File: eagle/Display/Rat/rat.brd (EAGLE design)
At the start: 99.2 x 116.2 mm, 72 parts, among them IC1 4511D, IC2 MEGA128-A, IC3 PCA82C250T, IC4 74LS138D, IC5 74LS138D, IC6 LM3914V, IC7 LM3914V, Q1 18.4320 MHz

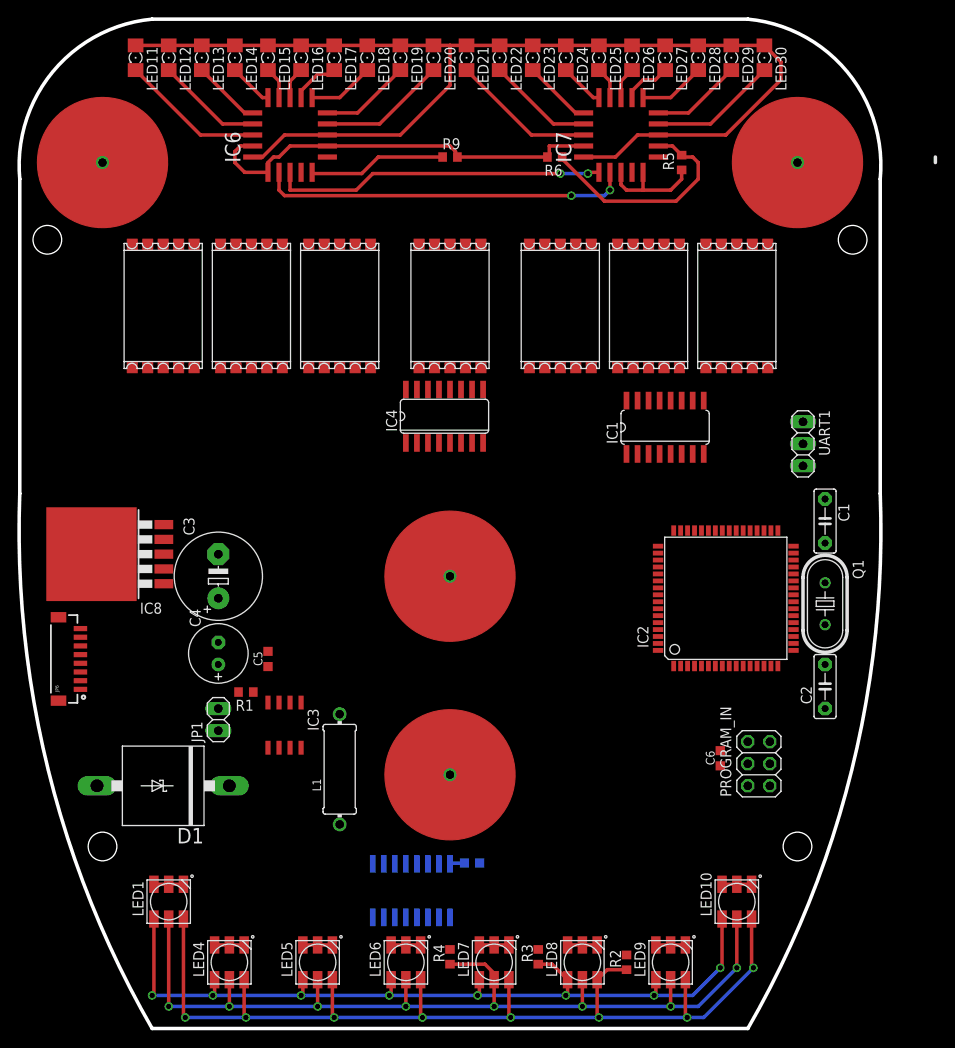
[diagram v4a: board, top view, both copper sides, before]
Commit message: changes to display layout
- Added shift light
- adjusted position of drillholes to take into account the size of the
buttons and the fotary switch
- added the connectors for the buttons (might have to be redonee)
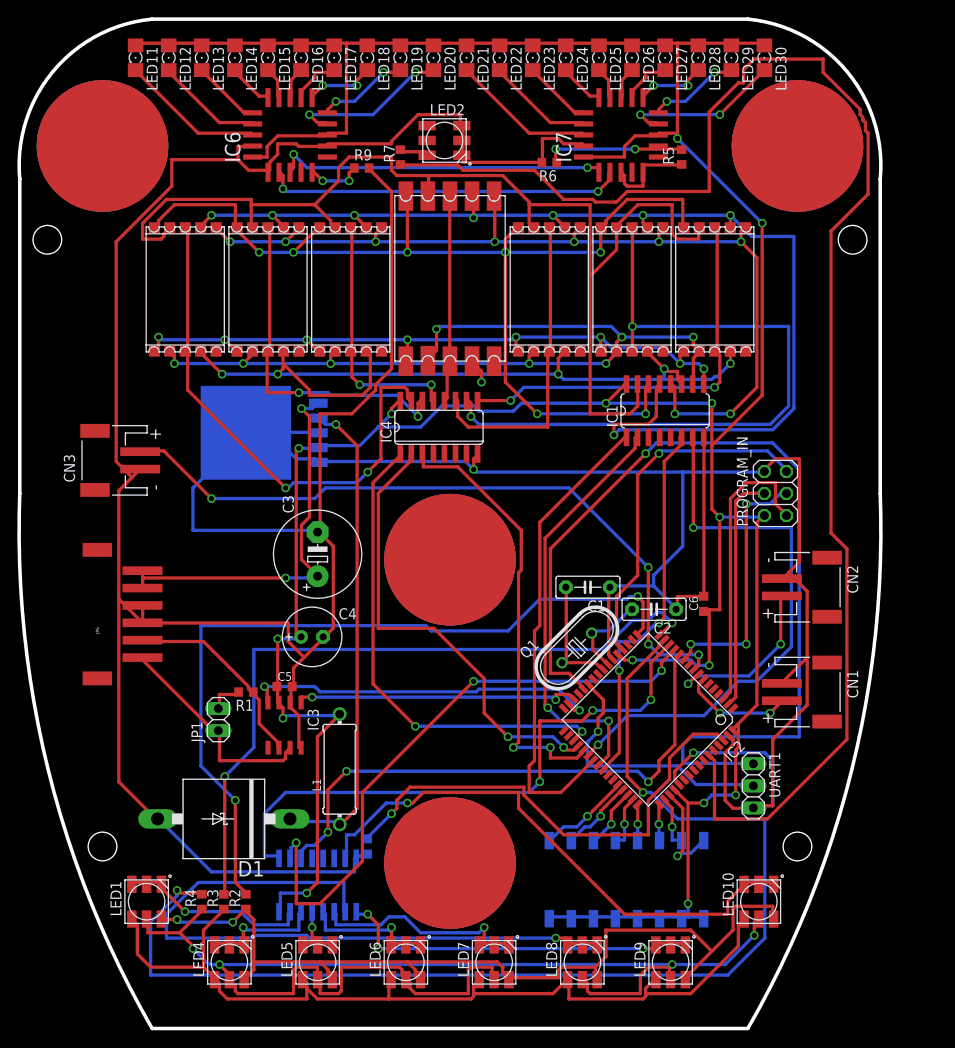
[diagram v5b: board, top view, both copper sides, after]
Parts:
- removed U$12, U$13, U$14, U$15: 15MM-DRILLHOLE, 15mm-drillhole:15MM-DRILLHOLE
- added CN1, CN2, CN3: (no value), adafruit:JST-PH-2-SMT-RA
- added LED2: RGBLED5050, adafruit:RGBLED5050
- added R7: 200, rcl:R0603
- added S1: SWS008, smd-special:SMS-008
- added U$1, U$10, U$11, U$9: 15MM-DRILLHOLE, big-drillhole:15MM-DRILLHOLE
- IC2: value MEGA128-A -> AT90CAN128
- JP6: value (none) -> M06; device SparkFun-Connectors:BM08B-SRSS-TB -> unicorn_v2:S6B_PH
- U$5: value REDSEVENSEGMENT -> BIGSEVENSEGMENT; device red_segment:REDSEGMENT -> red_segment:BIGSEVENSEGMENT
- moved R2 44.4 mm to (198.1, -17.1)
- moved UART1 39.8 mm to (256.5, -3.81)
- moved R3 36.7 mm to (195.6, -17.1)
- moved PROGRAM_IN 31.2 mm to (259.1, 29.8)
- moved R4 29.3 mm to (193.0, -17.1)
- moved Q1 29.0 mm to (236.2, 12.1), turned to 45 degrees
- moved C1 28.3 mm to (237.5, 19.1), turned to 180 degrees
- moved IC8 22.6 mm to (200.7, 36.8), flipped to the bottom, turned to 270 degrees
- moved C2 21.6 mm to (245.1, 16.5), turned to 180 degrees
- moved C6 17.9 mm to (250.8, 17.1)
- moved IC2 16.6 mm to (244.5, 3.81), turned to 225 degrees
- moved C19 12.2 mm to (212.1, -10.8), turned to 270 degrees
- moved C3 11.7 mm to (206.4, 22.9)
- moved C4 11.0 mm to (205.7, 13.3), turned to 0 degrees
- moved IC5 10.8 mm to (206.4, -15.2)
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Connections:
- new net N$11: IC2.47, S1.12
- new net N$4: IC2.44, S1.9
- new net N$44: IC2.48, S1.13
- new net N$46: IC2.49, S1.14
- new net N$47: IC2.50, S1.15
- new net N$5: IC2.45, S1.10
- new net N$69: IC2.51, S1.16
- new net N$7: IC2.46, S1.11
- new net N$70: CN1.1, IC2.7
- new net N$71: CN2.1, IC2.8
- new net N$77: CN3.1, IC2.9
- new net N$78: IC2.13, IC5.2
- new net N$79: IC2.12, IC5.3
- new net N$80: LED2.3, R7.2
- new net N$81: IC2.59, R7.1
- net +5V: now also S1.1, S1.2, S1.3, S1.4, S1.5, S1.6, S1.7, S1.8
- net N$19: now also U$5.GND2; no longer U$5.GN
- net N$41: now also IC2.16, R3.2; no longer IC2.7, R4.2
- net N$42: now also IC2.15, R4.2; no longer IC2.8, R3.2
- net N$43: now also IC2.14, IC5.1; no longer IC2.9, R2.2
- net N$9: now also R2.2
- net PE: now also CN1.2, CN2.2, CN3.2, LED2.4, LED2.5, LED2.6
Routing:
- net PE: track 49.7 -> 524.9 mm, vias 0 -> 2
- net +5V: track 134.3 -> 416.9 mm, vias 0 -> 15
- net N$81: track 0.00 -> 173.2 mm
- net N$42: track 0.00 -> 136.0 mm, vias 0 -> 2
- net N$3: track 0.00 -> 134.0 mm, vias 0 -> 8
- net N$14: track 0.00 -> 131.9 mm
- net N$15: track 0.00 -> 124.1 mm, vias 0 -> 7
- net TXD1: track 0.00 -> 108.7 mm, vias 0 -> 1
- net N$6: track 0.00 -> 108.1 mm, vias 0 -> 9
- net N$12: track 0.00 -> 100.5 mm, vias 0 -> 8
- net N$8: track 0.00 -> 98.2 mm, vias 0 -> 6
- net N$9: track 0.00 -> 90.2 mm, vias 0 -> 2
- net N$77: track 0.00 -> 82.1 mm, vias 0 -> 4
- net N$41: track 0.00 -> 82.0 mm, vias 0 -> 2
- net N$21: track 0.00 -> 81.4 mm, vias 0 -> 2
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
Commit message: changes
changes
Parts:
- C1, C2: value 22pF -> 22pf; device capacitor-wima:C5B2.5 -> rcl:C0603K
- moved R4 49.2 mm to (241.9, -22.9)
- moved R3 36.0 mm to (231.1, -22.9)
- moved R2 35.4 mm to (233.0, -22.9)
- moved CN3 20.3 mm to (182.9, 13.3)
- moved JP6 19.7 mm to (182.9, 35.6)
- moved C2 13.1 mm to (232.4, 13.3), flipped to the bottom, turned to 315 degrees
- moved C6 12.5 mm to (244.5, 6.35), flipped to the bottom, turned to 270 degrees
- moved IC1 8.82 mm to (241.9, 31.8)
- moved C1 4.96 mm to (234.3, 15.2), flipped to the bottom, turned to 135 degrees
- moved R5 2.84 mm to (247.0, 66.0)
- moved R6 2.84 mm to (234.3, 65.4)
- moved R7 2.29 mm to (214.6, 70.5), turned to 0 degrees
- moved R9 2.29 mm to (209.6, 66.0), turned to 90 degrees
- moved LED2 2.01 mm to (221.6, 72.4)
- moved IC4 2.01 mm to (221.0, 39.4)
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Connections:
- net +5V: now also IC1.5, IC4.6, IC5.6
- net N$1: now also C2.2; no longer C1.2
- net N$2: now also C1.2; no longer C2.2
- net PE: now also IC1.3, IC1.4, IC4.4, IC4.5, IC5.4, IC5.5
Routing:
- net TXD1: track 108.7 -> 24.0 mm
- net N$78: track 69.9 -> 143.9 mm, vias 3 -> 1
- net PE: track 524.9 -> 466.9 mm, vias 2 -> 3
- net N$43: track 68.0 -> 122.0 mm
- net N$81: track 173.2 -> 121.9 mm, vias 0 -> 2
- net N$42: track 136.0 -> 90.0 mm
- net N$21: track 81.4 -> 37.7 mm
- net N$9: track 90.2 -> 49.7 mm, vias 2 -> 4
- net N$38: track 79.1 -> 43.3 mm, vias 1 -> 3
- net N$41: track 82.0 -> 54.2 mm
- net +5V: track 416.9 -> 443.3 mm, vias 15 -> 7
- net N$32: track 102.6 -> 127.6 mm, vias 2 -> 3
- net N$3: track 134.0 -> 110.3 mm
- net N$26: track 64.0 -> 40.6 mm, vias 2 -> 4
- net N$6: track 108.1 -> 128.7 mm, vias 9 -> 4
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
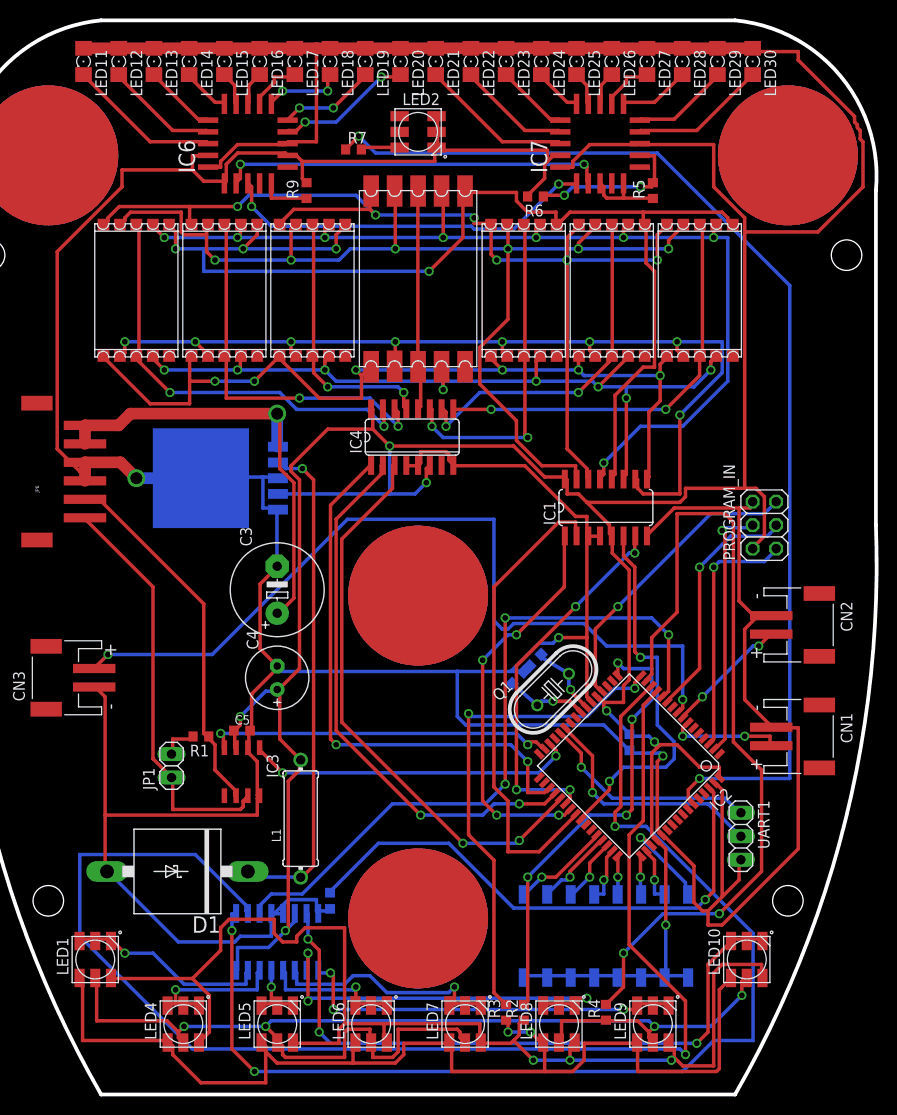
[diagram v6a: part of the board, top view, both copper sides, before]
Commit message: changes to the board
added the side mounted burn port
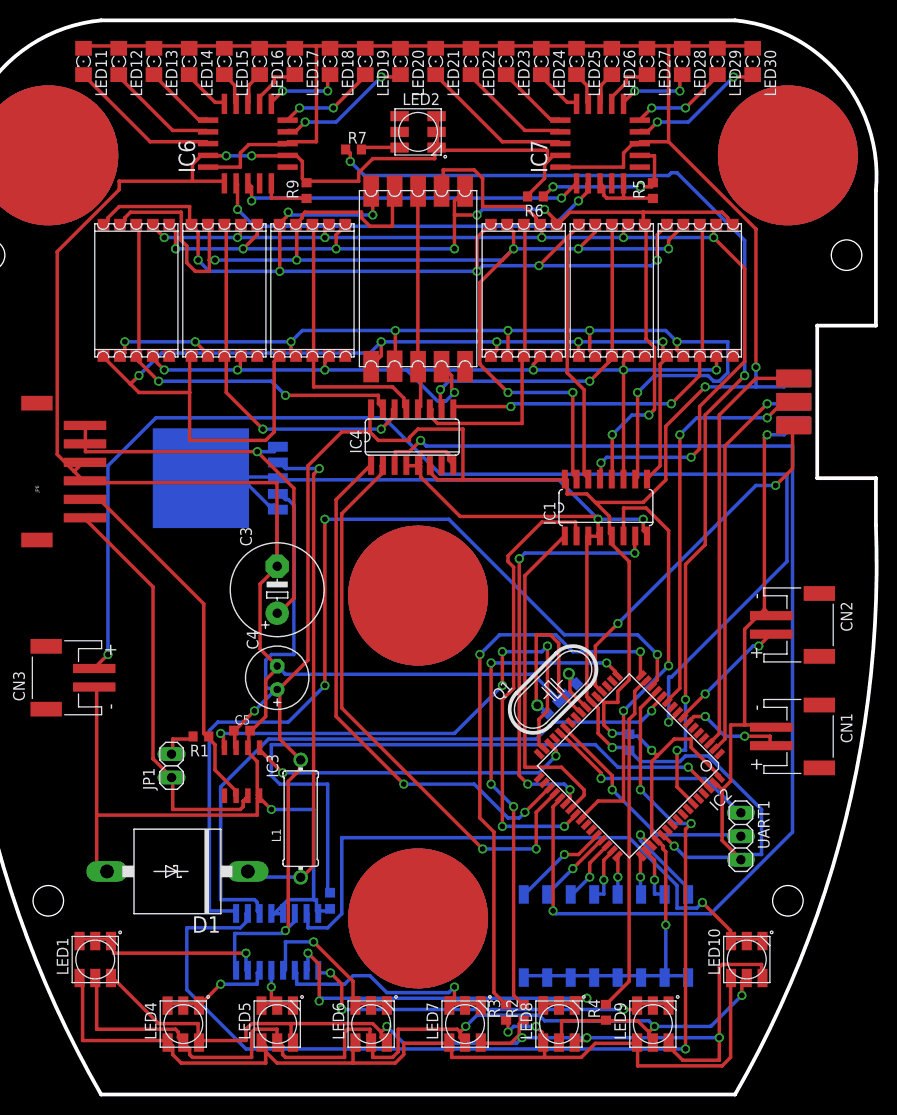
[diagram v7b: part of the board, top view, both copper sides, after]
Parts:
- removed PROGRAM_IN: (no value), pinhead:2X03
- added U$12: VERTPROGPORT, vertprogport:VERTPROGPORT
- moved C1 4.96 mm to (238.1, 12.1)
- moved C2 4.96 mm to (236.2, 10.2)
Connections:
- new net N$82: IC2.6
- net +5V: now also U$12.VCC; no longer PROGRAM_IN.2
- net MISO/TXD0: now also U$12.MISO; no longer PROGRAM_IN.1
- net MOSI/RXD0: now also U$12.MOSI; no longer PROGRAM_IN.4
- net PE: now also U$12.GND; no longer PROGRAM_IN.6
- net RESET: now also U$12.RESET; no longer PROGRAM_IN.5
- net SCK: now also U$12.SCK; no longer PROGRAM_IN.3
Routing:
- net N$25: track 61.3 -> 129.1 mm
- net N$42: track 90.0 -> 37.0 mm, vias 2 -> 0
- net N$77: track 90.4 -> 134.4 mm
- net N$78: track 143.9 -> 114.1 mm, vias 1 -> 3
- net N$13: track 94.0 -> 120.1 mm, vias 6 -> 5
- net N$43: track 122.0 -> 100.8 mm
- net N$32: track 127.6 -> 107.9 mm, vias 3 -> 4
- net MISO/TXD0: track 26.9 -> 45.7 mm, vias 1 -> 0
- net PE: track 466.9 -> 484.7 mm, vias 3 -> 8
- net N$6: track 128.7 -> 110.9 mm, vias 4 -> 8
- net +5V: track 443.3 -> 425.5 mm
- net N$14: track 118.4 -> 135.5 mm, vias 6 -> 7
- net RXCAN: track 37.9 -> 55.0 mm, vias 2 -> 4
- net SCK: track 26.3 -> 43.2 mm, vias 1 -> 2
- net N$30: track 128.5 -> 112.3 mm, vias 4 -> 3
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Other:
- outline, holes or cut-outs redrawn

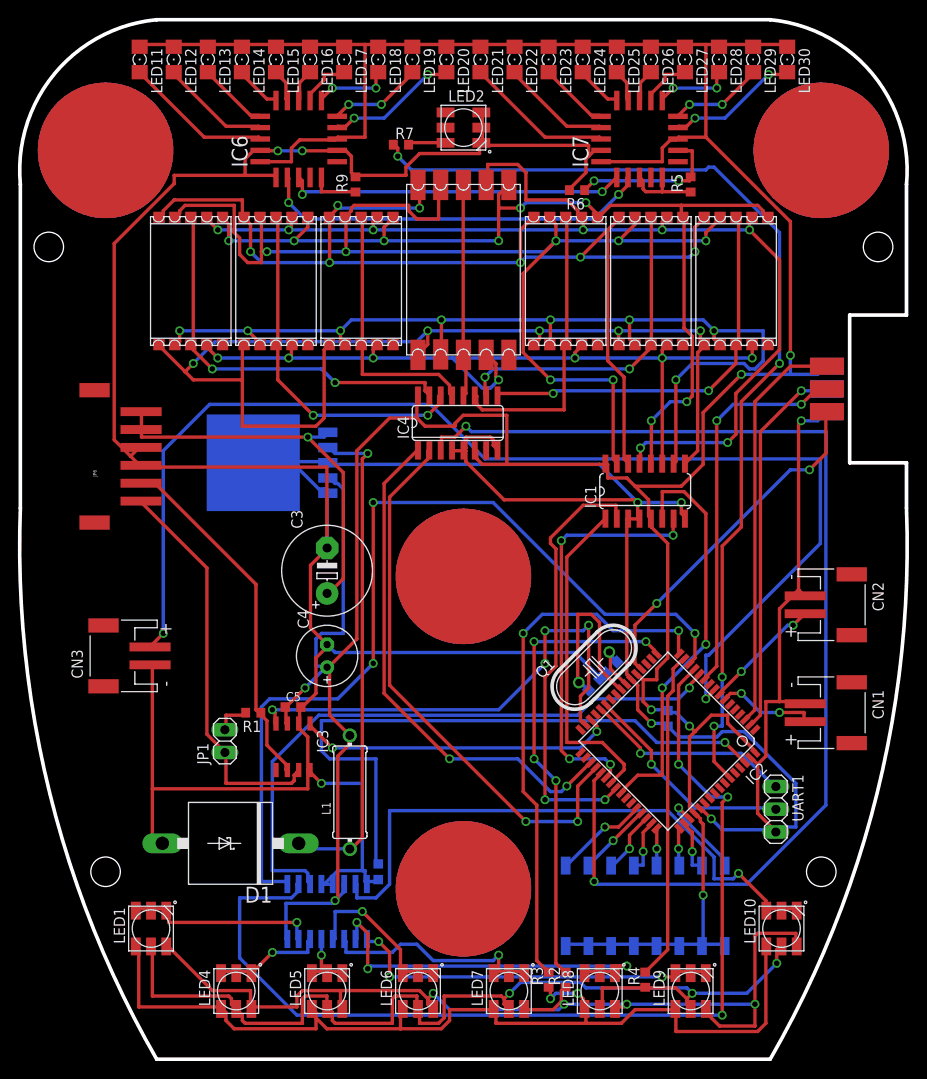
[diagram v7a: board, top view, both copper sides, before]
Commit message: added pull down resistors to buttons
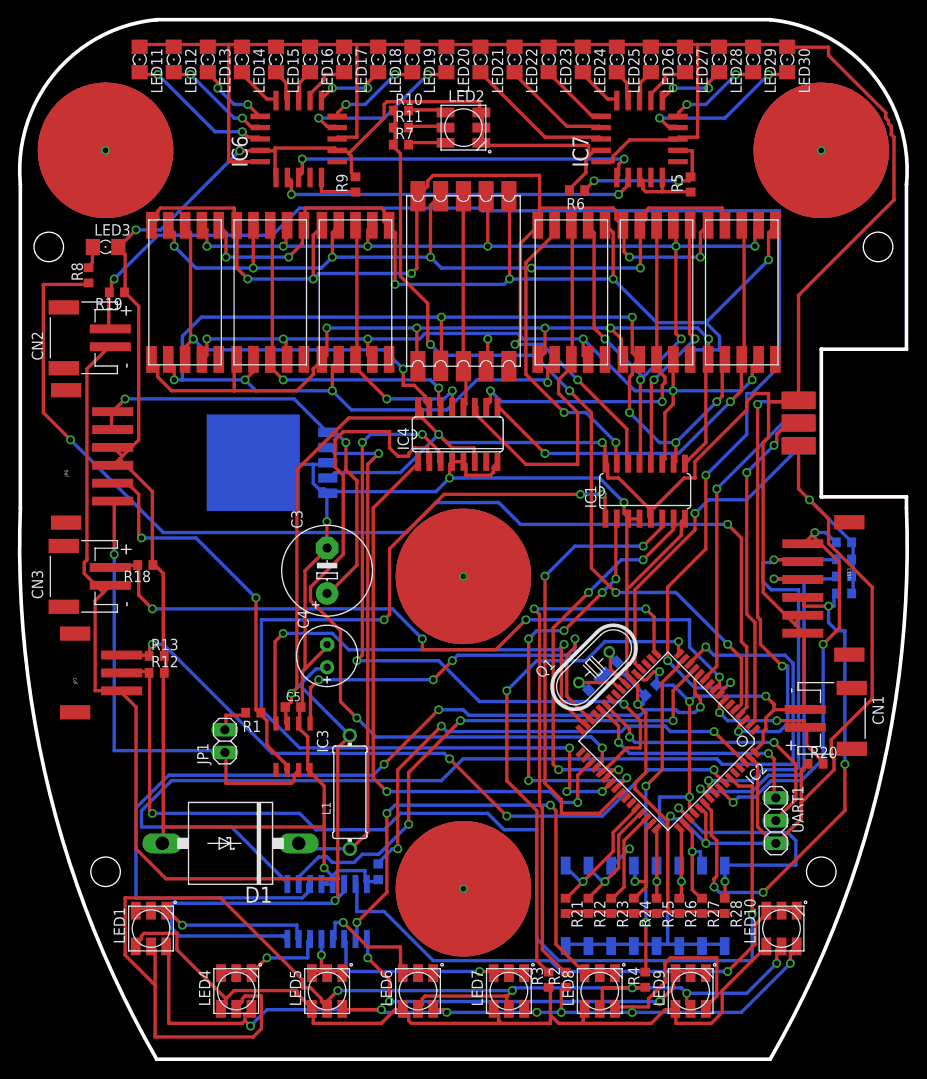
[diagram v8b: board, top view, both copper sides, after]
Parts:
- added JP7: (no value), unicorn_v2:S3B-PH
- added LED3: GREEN, led:1206
- added R10, R11, R12, R13, R14, R15, R16, R17, R18, R19, R20, R21, R22, R23, R24, R25, R26, R27, R28, R8: 200, rcl:R0603
- added U$13: M06, unicorn_v2:S6B_PH
- moved CN2 90.2 mm to (178.4, 48.9), turned to 90 degrees
- moved CN3 9.94 mm to (178.4, 22.2)
- moved U$12 4.96 mm to (259.1, 39.4), flipped to the bottom
- moved C6 3.70 mm to (242.6, 9.53), turned to 315 degrees
- moved JP6 3.17 mm to (179.7, 35.6)
- moved U$6 1.42 mm to (233.7, 54.0)
- moved U$7 1.42 mm to (243.2, 54.0)
- moved U$2 1.42 mm to (190.5, 54.0)
- moved U$3 1.42 mm to (200.0, 54.0)
- moved U$4 1.42 mm to (209.6, 54.0)
- moved U$8 1.42 mm to (252.7, 54.0)
- moved U$5 1.27 mm to (221.6, 55.2)
- moved UART1 1.27 mm to (256.5, -5.08)
- moved IC4 1.27 mm to (221.0, 38.1)
- moved CN1 0.64 mm to (263.5, 6.35)
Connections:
- new net N$83: IC2.57, R14.1, U$13.1
- new net N$84: IC2.56, R15.1, U$13.2
- new net N$85: IC2.55, R16.1, U$13.3
- new net N$86: IC2.54, R17.1, U$13.4
- new net N$87: LED2.1, R10.2
- new net N$88: LED3.A, R8.2
- new net N$89: IC2.4, R8.1
- new net N$90: LED2.2, R11.2
- new net N$91: IC2.58, JP7.3, R13.1
- new net N$92: IC2.59, JP7.2, R12.1
- net +5V: now also CN1.2, CN2.2, CN3.2, JP7.1, U$13.5, U$13.6
- net N$11: now also R24.1
- net N$16: now also U$2.GND2; no longer U$2.GN
- net N$17: now also U$3.GND2; no longer U$3.GN
- net N$18: now also U$4.GND2; no longer U$4.GN
- net N$20: now also U$6.GND2; no longer U$6.GN
- net N$21: now also U$7.GND2; no longer U$7.GN
- net N$22: now also U$8.GND2; no longer U$8.GN
- net N$4: now also R21.1
- net N$44: now also R25.1
- net N$46: now also R26.1
- net N$47: now also R27.1
- net N$5: now also R22.1
- net N$69: now also R28.1
- net N$7: now also R23.1
- net N$70: now also R20.2
- net N$71: now also R19.2
- net N$77: now also R18.2
- net N$81: now also IC2.5, R10.1, R11.1; no longer IC2.59
- net PE: now also LED3.C, R12.2, R13.2, R14.2, R15.2, R16.2, R17.2, R18.1, R19.1, R20.1, R21.2, R22.2, R23.2, R24.2, R25.2, R26.2, R27.2, R28.2; no longer CN1.2, CN2.2, CN3.2
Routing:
- net +5V: track 425.5 -> 583.0 mm, vias 7 -> 8
- net N$71: track 13.4 -> 149.9 mm, vias 2 -> 4
- net N$89: track 0.00 -> 126.3 mm, vias 0 -> 2
- net N$92: track 0.00 -> 124.0 mm, vias 0 -> 2
- net N$91: track 0.00 -> 79.4 mm, vias 0 -> 4
- net N$27: track 36.9 -> 107.7 mm, vias 0 -> 6
- net N$86: track 0.00 -> 58.8 mm, vias 0 -> 4
- net N$78: track 114.1 -> 60.5 mm
- net N$77: track 134.4 -> 82.3 mm, vias 2 -> 4
- net N$25: track 129.1 -> 78.8 mm, vias 2 -> 4
- net N$84: track 0.00 -> 50.3 mm, vias 0 -> 2
- net N$83: track 0.00 -> 46.1 mm, vias 0 -> 3
- net N$85: track 0.00 -> 45.8 mm, vias 0 -> 2
- net N$12: track 107.7 -> 150.3 mm, vias 8 -> 9
- net N$30: track 112.3 -> 147.9 mm, vias 3 -> 5
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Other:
- outline, holes or cut-outs redrawn
